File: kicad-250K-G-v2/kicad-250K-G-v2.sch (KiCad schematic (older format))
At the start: 28 parts, among them P1 In, P2 Out, P3 Power, U1 TL072

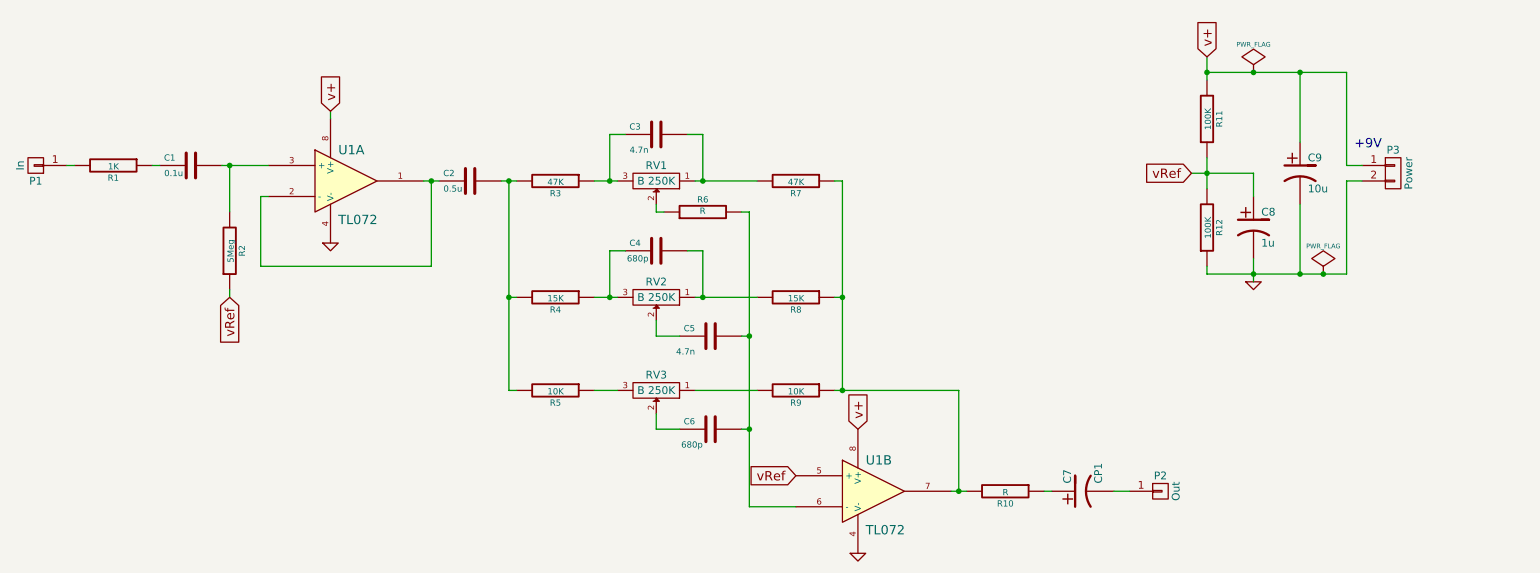
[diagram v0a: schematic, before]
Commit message: started pcb layout
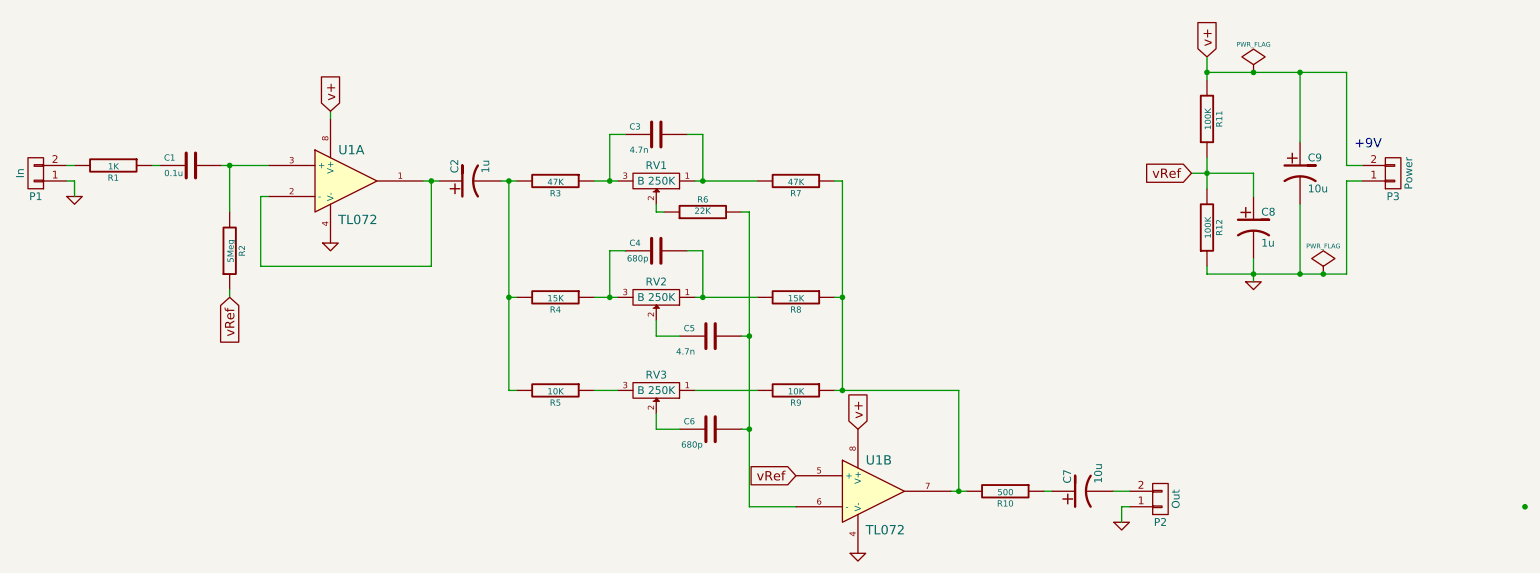
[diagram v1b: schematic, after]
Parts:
- removed C2: 0.5u, symbol C
- removed P1: In, symbol CONN_01X01
- removed P2: Out, symbol CONN_01X01
- added C2: 1u, Custom:C1.5V7-LARGE_PADS, symbol CP1
- added P1: In, Custom:SIL-2-LARGE_PADS, symbol CONN_01X02
- added P2: Out, Custom:SIL-2-LARGE_PADS, symbol CONN_01X02
- C1, C3, C4, C5, C6: footprint (none) -> Custom:C2-LARGE_PADS
- C7: value CP1 -> 10u; footprint (none) -> Custom:C1.5V7-LARGE_PADS
- C8, C9: footprint (none) -> Custom:C1.5V7-LARGE_PADS
- P3: footprint (none) -> Custom:SIL-2-LARGE_PADS
- R1, R11, R12, R2, R3, R4, R5, R7, R8, R9: footprint (none) -> Custom:R3-LARGE_PADS
- R10: value R -> 500; footprint (none) -> Custom:R3-LARGE_PADS
- R6: value R -> 22K; footprint (none) -> Custom:R3-LARGE_PADS
- RV1, RV2, RV3: footprint (none) -> Custom:SIL-3-LARGE_PADS
- U1: footprint (none) -> Custom:DIP-8_LARGE_PADS
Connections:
- net GND: now also P3.1 (P1), P1.1 (P1), P2.1 (P1); no longer P3.2 (P2)
- net v+: now also P3.2 (P2); no longer P3.1 (P1)
- net at U1.1, U1.2 (-): now also C2.1
- net at R1.2: now also P1.2 (P2)
- net at R3.2, R4.2, R5.2: now also C2.2
- net at C7.2: now also P2.2 (P2)
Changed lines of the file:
@@
 LIBS:valves
 LIBS:linear
+LIBS:kicad-250K-G-v2-cache
 EELAYER 24 0
 EELAYER END
@@
 encoding utf-8
 Sheet 1 1
-Title ""
-Date ""
-Rev ""
-Comp ""
-Comment1 ""
+Title "Preamp 3EQ \"Lutherie Amateur\""
+Date "27 August 2014"
+Rev "V2"
+Comp "www.dolganoff.com"
+Comment1 "Guitar version, 250K pots"
 Comment2 ""
 Comment3 ""
@@
 F 0 "U1" H 3050 2950 60  0000 L CNN
 F 1 "TL072" H 3050 2500 60  0000 L CNN
-F 2 "" H 3100 2750 60  0000 C CNN
+F 2 "Custom:DIP-8_LARGE_PADS" H 3100 2750 60  0001 C CNN
 F 3 "" H 3100 2750 60  0000 C CNN
 	1    3100 2750
@@
 F 0 "U1" H 6450 4950 60  0000 L CNN
 F 1 "TL072" H 6450 4500 60  0000 L CNN
-F 2 "" H 6500 4750 60  0000 C CNN
+F 2 "Custom:DIP-8_LARGE_PADS" H 6500 4750 60  0001 C CNN
 F 3 "" H 6500 4750 60  0000 C CNN
 	2    6500 4750
@@
 F 0 "R1" V 1680 2650 40  0000 C CNN
 F 1 "1K" V 1607 2651 40  0000 C CNN
-F 2 "" V 1530 2650 30  0000 C CNN
+F 2 "Custom:R3-LARGE_PADS" V 1530 2650 30  0001 C CNN
 F 3 "" H 1600 2650 30  0000 C CNN
 	1    1600 2650
@@
 F 0 "C1" V 2150 2750 40  0000 L CNN
 F 1 "0.1u" V 2050 2700 40  0000 L CNN
-F 2 "" H 2138 2500 30  0000 C CNN
+F 2 "Custom:C2-LARGE_PADS" H 2138 2500 30  0001 C CNN
 F 3 "" H 2100 2650 60  0000 C CNN
 	1    2100 2650
@@
 F 0 "R2" V 2430 3200 40  0000 C CNN
 F 1 "5Meg" V 2357 3201 40  0000 C CNN
-F 2 "" V 2280 3200 30  0000 C CNN
+F 2 "Custom:R3-LARGE_PADS" V 2280 3200 30  0001 C CNN
 F 3 "" H 2350 3200 30  0000 C CNN
 	1    2350 3200
 	1    0    0    1
-$EndComp
-$Comp
-L CONN_01X01 P1
-U 1 1 53FDBD33
-P 1100 2650
-F 0 "P1" H 1100 2750 50  0000 C CNN
-F 1 "In" V 1200 2650 50  0000 C CNN
-F 2 "" H 1100 2650 60  0000 C CNN
-F 3 "" H 1100 2650 60  0000 C CNN
-	1    1100 2650
-	-1   0    0    1
 $EndComp
 Text GLabel 2350 3500 3    60   Input ~ 0
@@
 v+
 $Comp
-L C C2
-U 1 1 53FDBFCB
-P 3900 2750
-F 0 "C2" V 3950 2850 40  0000 L CNN
-F 1 "0.5u" V 3850 2800 40  0000 L CNN
-F 2 "" H 3938 2600 30  0000 C CNN
-F 3 "" H 3900 2750 60  0000 C CNN
-	1    3900 2750
-	0    -1   -1   0
-$EndComp
-$Comp
 L R R3
 U 1 1 53FDC007
@@
 F 0 "R3" V 4530 2750 40  0000 C CNN
 F 1 "47K" V 4457 2751 40  0000 C CNN
-F 2 "" V 4380 2750 30  0000 C CNN
+F 2 "Custom:R3-LARGE_PADS" V 4380 2750 30  0001 C CNN
 F 3 "" H 4450 2750 30  0000 C CNN
 	1    4450 2750
@@
 F 0 "R4" V 4530 3500 40  0000 C CNN
 F 1 "15K" V 4457 3501 40  0000 C CNN
-F 2 "" V 4380 3500 30  0000 C CNN
+F 2 "Custom:R3-LARGE_PADS" V 4380 3500 30  0001 C CNN
 F 3 "" H 4450 3500 30  0000 C CNN
 	1    4450 3500
@@
 F 0 "R9" V 6080 4100 40  0000 C CNN
 F 1 "10K" V 6007 4101 40  0000 C CNN
-F 2 "" V 5930 4100 30  0000 C CNN
+F 2 "Custom:R3-LARGE_PADS" V 5930 4100 30  0001 C CNN
 F 3 "" H 6000 4100 30  0000 C CNN
 	1    6000 4100
@@
 F 0 "RV1" H 5100 2650 50  0000 C CNN
 F 1 "B 250K" H 5100 2750 50  0000 C CNN
-F 2 "" H 5100 2750 60  0000 C CNN
+F 2 "Custom:SIL-3-LARGE_PADS" H 5100 2750 60  0001 C CNN
 F 3 "" H 5100 2750 60  0000 C CNN
 	1    5100 2750
@@
 F 0 "C3" V 5150 2550 40  0000 L CNN
 F 1 "4.7n" V 5000 2500 40  0000 L CNN
-F 2 "" H 5138 2300 30  0000 C CNN
+F 2 "Custom:C2-LARGE_PADS" H 5138 2300 30  0001 C CNN
 F 3 "" H 5100 2450 60  0000 C CNN
 	1    5100 2450
@@
 F 0 "R7" V 6080 2750 40  0000 C CNN
 F 1 "47K" V 6007 2751 40  0000 C CNN
-F 2 "" V 5930 2750 30  0000 C CNN
+F 2 "Custom:R3-LARGE_PADS" V 5930 2750 30  0001 C CNN
 F 3 "" H 6000 2750 30  0000 C CNN
 	1    6000 2750
@@
 F 0 "C4" V 5150 3300 40  0000 L CNN
 F 1 "680p" V 5050 3250 40  0000 L CNN
-F 2 "" H 5138 3050 30  0000 C CNN
+F 2 "Custom:C2-LARGE_PADS" H 5138 3050 30  0001 C CNN
 F 3 "" H 5100 3200 60  0000 C CNN
 	1    5100 3200
@@
 F 0 "RV2" H 5100 3400 50  0000 C CNN
 F 1 "B 250K" H 5100 3500 50  0000 C CNN
-F 2 "" H 5100 3500 60  0000 C CNN
+F 2 "Custom:SIL-3-LARGE_PADS" H 5100 3500 60  0001 C CNN
 F 3 "" H 5100 3500 60  0000 C CNN
 	1    5100 3500
@@
 F 0 "R8" V 6080 3500 40  0000 C CNN
 F 1 "15K" V 6007 3501 40  0000 C CNN
-F 2 "" V 5930 3500 30  0000 C CNN
+F 2 "Custom:R3-LARGE_PADS" V 5930 3500 30  0001 C CNN
 F 3 "" H 6000 3500 30  0000 C CNN
 	1    6000 3500
@@
 P 5400 2950
 F 0 "R6" V 5480 2950 40  0000 C CNN
-F 1 "R" V 5407 2951 40  0000 C CNN
-F 2 "" V 5330 2950 30  0000 C CNN
+F 1 "22K" V 5407 2951 40  0000 C CNN
+F 2 "Custom:R3-LARGE_PADS" V 5330 2950 30  0001 C CNN
 F 3 "" H 5400 2950 30  0000 C CNN
 	1    5400 2950
@@
 F 0 "RV3" H 5100 4000 50  0000 C CNN
 F 1 "B 250K" H 5100 4100 50  0000 C CNN
-F 2 "" H 5100 4100 60  0000 C CNN
+F 2 "Custom:SIL-3-LARGE_PADS" H 5100 4100 60  0001 C CNN
 F 3 "" H 5100 4100 60  0000 C CNN
 	1    5100 4100
@@
 F 0 "C5" V 5500 3850 40  0000 L CNN
 F 1 "4.7n" V 5350 3850 40  0000 L CNN
-F 2 "" H 5488 3600 30  0000 C CNN
+F 2 "Custom:C2-LARGE_PADS" H 5488 3600 30  0001 C CNN
 F 3 "" H 5450 3750 60  0000 C CNN
 	1    5450 3750
@@
 F 0 "R5" V 4530 4100 40  0000 C CNN
 F 1 "10K" V 4457 4101 40  0000 C CNN
-F 2 "" V 4380 4100 30  0000 C CNN
+F 2 "Custom:R3-LARGE_PADS" V 4380 4100 30  0001 C CNN
 F 3 "" H 4450 4100 30  0000 C CNN
 	1    4450 4100
@@
 F 0 "C6" V 5500 4450 40  0000 L CNN
 F 1 "680p" V 5350 4400 40  0000 L CNN
-F 2 "" H 5488 4200 30  0000 C CNN
+F 2 "Custom:C2-LARGE_PADS" H 5488 4200 30  0001 C CNN
 F 3 "" H 5450 4350 60  0000 C CNN
 	1    5450 4350
@@
 P 7350 4750
 F 0 "R10" V 7430 4750 40  0000 C CNN
-F 1 "R" V 7357 4751 40  0000 C CNN
-F 2 "" V 7280 4750 30  0000 C CNN
+F 1 "500" V 7357 4751 40  0000 C CNN
+F 2 "Custom:R3-LARGE_PADS" V 7280 4750 30  0001 C CNN
 F 3 "" H 7350 4750 30  0000 C CNN
 	1    7350 4750
@@
 P 7850 4750
 F 0 "C7" H 7900 4850 50  0000 L CNN
-F 1 "CP1" H 7900 4650 50  0000 L CNN
-F 2 "" H 7850 4750 60  0000 C CNN
+F 1 "10u" H 7900 4650 50  0000 L CNN
+F 2 "Custom:C1.5V7-LARGE_PADS" H 7850 4750 60  0001 C CNN
 F 3 "" H 7850 4750 60  0000 C CNN
 	1    7850 4750
@@
 F 0 "R11" V 8730 2350 40  0000 C CNN
 F 1 "100K" V 8657 2351 40  0000 C CNN
-F 2 "" V 8580 2350 30  0000 C CNN
+F 2 "Custom:R3-LARGE_PADS" V 8580 2350 30  0001 C CNN
 F 3 "" H 8650 2350 30  0000 C CNN
 	1    8650 2350
@@
 F 0 "R12" V 8730 3050 40  0000 C CNN
 F 1 "100K" V 8657 3051 40  0000 C CNN
-F 2 "" V 8580 3050 30  0000 C CNN
+F 2 "Custom:R3-LARGE_PADS" V 8580 3050 30  0001 C CNN
 F 3 "" H 8650 3050 30  0000 C CNN
 	1    8650 3050
@@
 F 0 "C8" H 9000 3150 50  0000 L CNN
 F 1 "1u" H 9000 2950 50  0000 L CNN
-F 2 "" H 8950 3050 60  0000 C CNN
+F 2 "Custom:C1.5V7-LARGE_PADS" H 8950 3050 60  0001 C CNN
 F 3 "" H 8950 3050 60  0000 C CNN
 	1    8950 3050
-	1    0    0    -1
-$EndComp
-$Comp
-L CONN_01X01 P2
-U 1 1 53FDFA95
-P 8350 4750
-F 0 "P2" H 8350 4850 50  0000 C CNN
-F 1 "Out" V 8450 4750 50  0000 C CNN
-F 2 "" H 8350 4750 60  0000 C CNN
-F 3 "" H 8350 4750 60  0000 C CNN
-	1    8350 4750
 	1    0    0    -1
 $EndComp
@@
 F 0 "C9" H 9300 2800 50  0000 L CNN
 F 1 "10u" H 9300 2600 50  0000 L CNN
-F 2 "" H 9250 2700 60  0000 C CNN
+F 2 "Custom:C1.5V7-LARGE_PADS" H 9250 2700 60  0001 C CNN
 F 3 "" H 9250 2700 60  0000 C CNN
 	1    9250 2700
@@
 F 0 "P3" H 9850 2850 50  0000 C CNN
 F 1 "Power" V 9950 2700 50  0000 C CNN
-F 2 "" H 9850 2700 60  0000 C CNN
+F 2 "Custom:SIL-2-LARGE_PADS" H 9850 2700 60  0001 C CNN
 F 3 "" H 9850 2700 60  0000 C CNN
 	1    9850 2700
-	1    0    0    -1
+	1    0    0    1
 $EndComp
 Wire Wire Line
@@
 	7650 4750 7600 4750
 Wire Wire Line
-	8650 2800 8650 2600
+	8650 2600 8650 2800
 Wire Wire Line
 	8150 4750 8050 4750
@@
 	8950 3250 8950 3400
 Wire Wire Line
-	9250 2500 9250 2050
+	9250 2050 9250 2500
 Wire Wire Line
 	8650 2050 9550 2050
@@
 Text Notes 9600 2550 0    60   ~ 0
 +9V
+$Comp
+L CP1 C2
+U 1 1 53FE7685
+P 3900 2750
+F 0 "C2" H 3950 2850 50  0000 L CNN
+F 1 "1u" H 3950 2650 50  0000 L CNN
+F 2 "Custom:C1.5V7-LARGE_PADS" H 3900 2750 60  0001 C CNN
+F 3 "" H 3900 2750 60  0000 C CNN
+	1    3900 2750
+	0    -1   -1   0
+$EndComp
+Connection ~ 10700 4850
+$Comp
+L CONN_01X02 P2
+U 1 1 53FDE8A1
+P 8350 4800
+F 0 "P2" H 8350 4950 50  0000 C CNN
+F 1 "Out" V 8450 4800 50  0000 C CNN
+F 2 "Custom:SIL-2-LARGE_PADS" H 8350 4800 60  0001 C CNN
+F 3 "" H 8350 4800 60  0000 C CNN
+	1    8350 4800
+	1    0    0    1
+$EndComp
+$Comp
+L GND #PWR06
+U 1 1 53FDE947
+P 8100 4950
+F 0 "#PWR06" H 8100 4950 30  0001 C CNN
+F 1 "GND" H 8100 4880 30  0001 C CNN
+F 2 "" H 8100 4950 60  0000 C CNN
+F 3 "" H 8100 4950 60  0000 C CNN
+	1    8100 4950
+	1    0    0    -1
+$EndComp
+Wire Wire Line
+	8100 4950 8100 4850
+Wire Wire Line
+	8100 4850 8150 4850
+$Comp
+L CONN_01X02 P1
+U 1 1 53FDEDC6
+P 1100 2700
+F 0 "P1" H 1100 2850 50  0000 C CNN
+F 1 "In" V 1200 2700 50  0000 C CNN
+F 2 "Custom:SIL-2-LARGE_PADS" H 1100 2700 60  0001 C CNN
+F 3 "" H 1100 2700 60  0000 C CNN
+	1    1100 2700
+	-1   0    0    1
+$EndComp
+$Comp
+L GND #PWR?
+U 1 1 53FDEE90
+P 1350 2850
+F 0 "#PWR?" H 1350 2850 30  0001 C CNN
+F 1 "GND" H 1350 2780 30  0001 C CNN
+F 2 "" H 1350 2850 60  0000 C CNN
+F 3 "" H 1350 2850 60  0000 C CNN
+	1    1350 2850
+	1    0    0    -1
+$EndComp
+Wire Wire Line
+	1350 2850 1350 2750
+Wire Wire Line
+	1350 2750 1300 2750
 $EndSCHEMATC

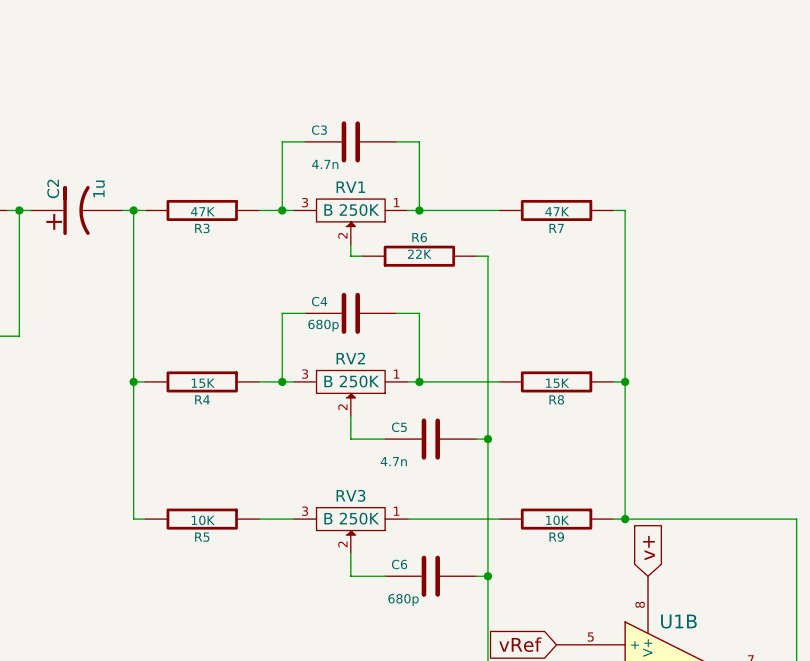
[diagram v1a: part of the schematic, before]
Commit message: pcb routed
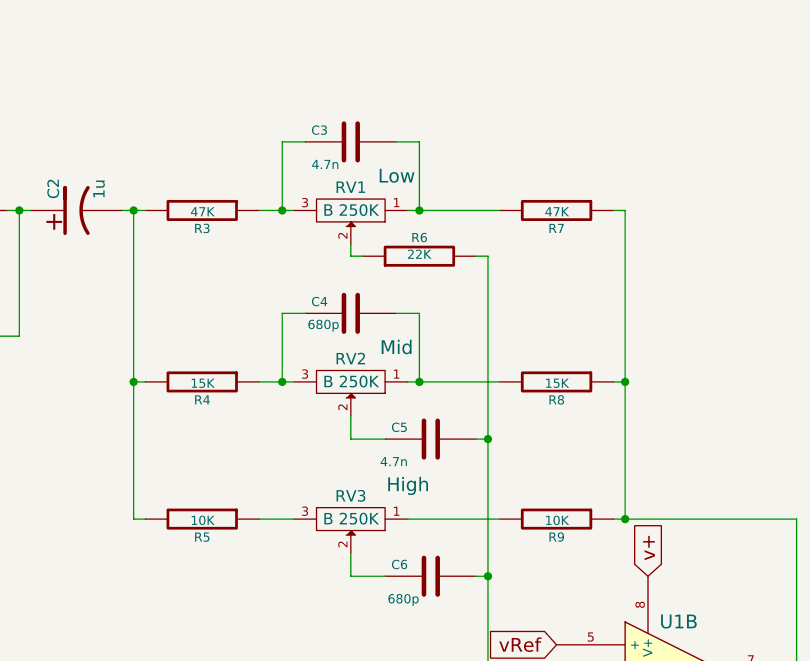
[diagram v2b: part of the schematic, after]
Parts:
- RV1: Field4 (none) -> Low
- RV2: Field4 (none) -> Mid
- RV3: Field4 (none) -> High
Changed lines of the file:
@@
 F 2 "Custom:SIL-3-LARGE_PADS" H 5100 2750 60  0001 C CNN
 F 3 "" H 5100 2750 60  0000 C CNN
+F 4 "Low" H 4900 2600 60  0000 C CNN "Field4"
 	1    5100 2750
 	-1   0    0    1
@@
 F 2 "Custom:SIL-3-LARGE_PADS" H 5100 3500 60  0001 C CNN
 F 3 "" H 5100 3500 60  0000 C CNN
+F 4 "Mid" H 4900 3350 60  0000 C CNN "Field4"
 	1    5100 3500
 	-1   0    0    1
@@
 F 2 "Custom:SIL-3-LARGE_PADS" H 5100 4100 60  0001 C CNN
 F 3 "" H 5100 4100 60  0000 C CNN
+F 4 "High" H 4850 3950 60  0000 C CNN "Field4"
 	1    5100 4100
 	-1   0    0    1

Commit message: routing corrections
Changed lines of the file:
@@
 	0    -1   -1   0
 $EndComp
-Connection ~ 10700 4850
 $Comp
 L CONN_01X02 P2
